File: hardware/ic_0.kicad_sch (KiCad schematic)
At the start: 24 parts, among them IC1 BTS722204ESAXUMA1

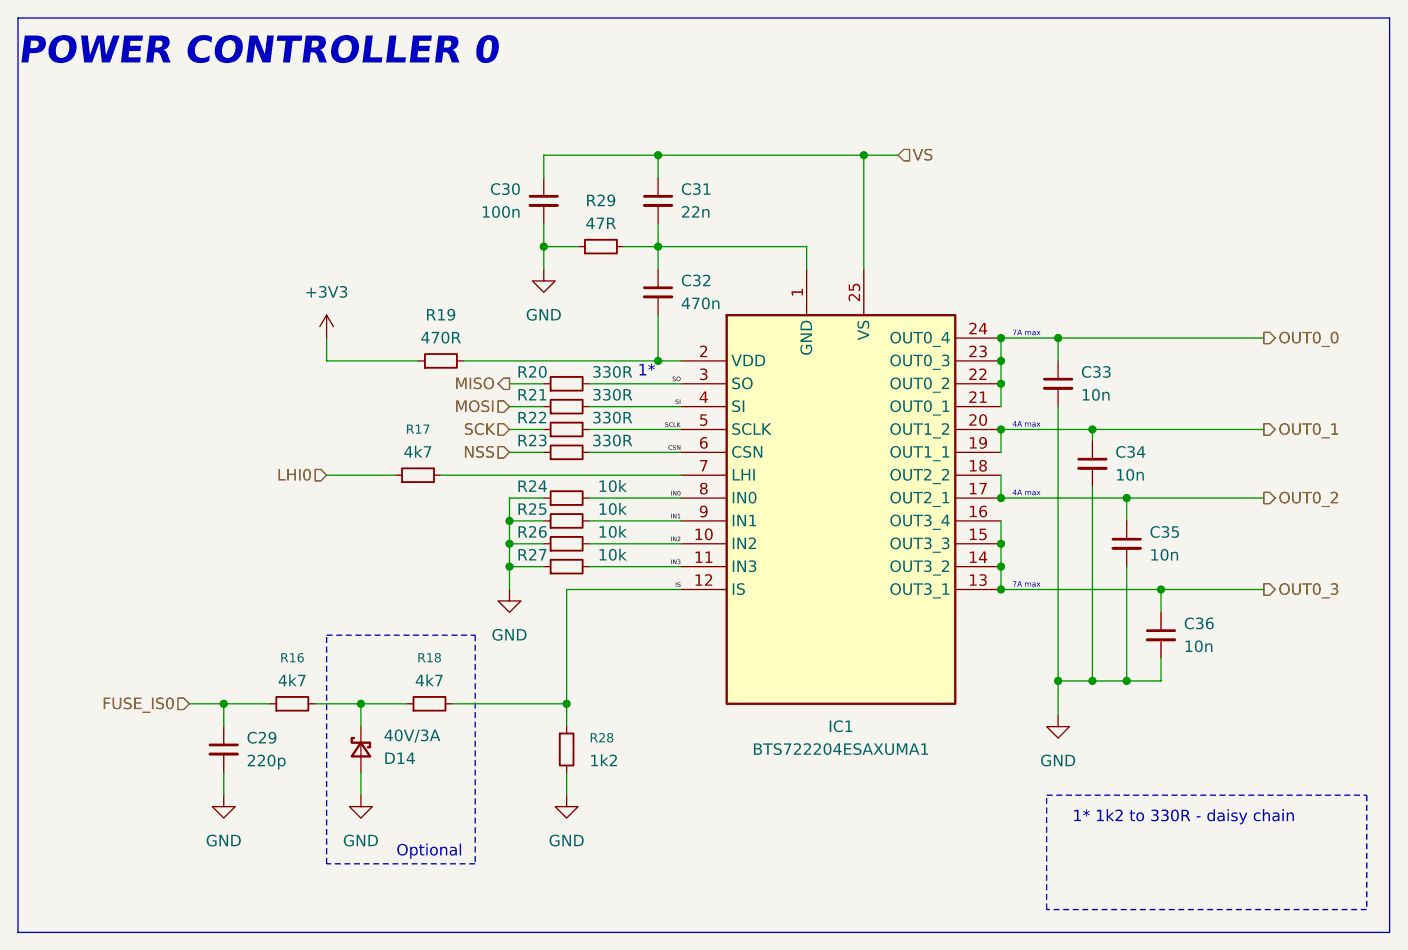
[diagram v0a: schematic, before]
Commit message: new pcb layout & can coppied from steeringwheel
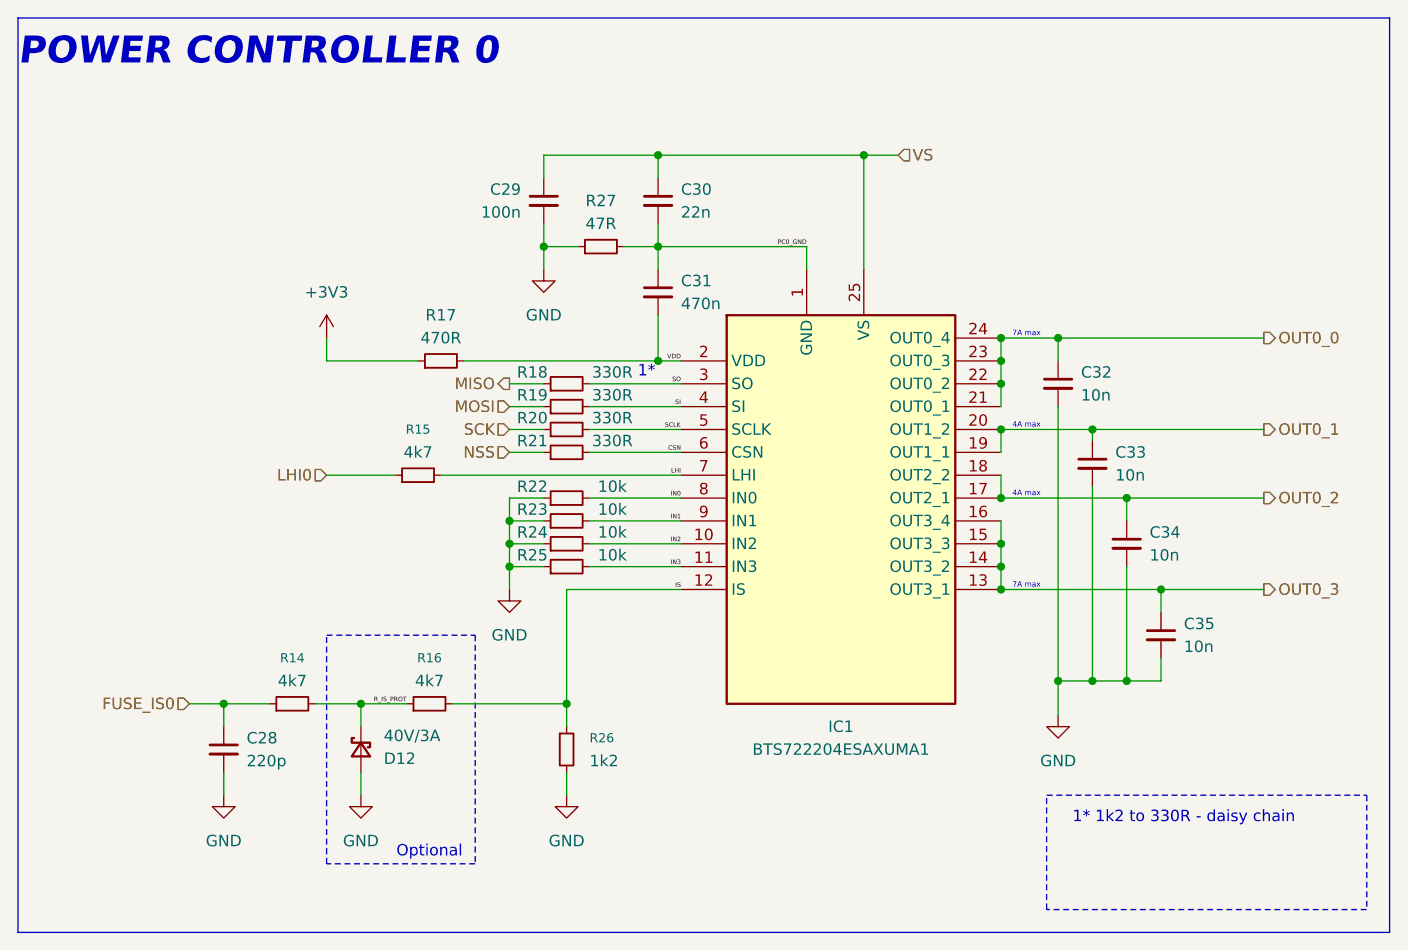
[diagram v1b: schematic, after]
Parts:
- renumbered C29 to C28, C30 to C29, C31 to C30, C32 to C31, C33 to C32, C34 to C33, C35 to C34, C36 to C35, D14 to D12, R16 to R14, R17 to R15, R18 to R16, R19 to R17, R20 to R18, R21 to R19, R22 to R20, R23 to R21, R24 to R22, R25 to R23, R26 to R24, R27 to R25, R28 to R26, R29 to R27
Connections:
- net R_IS_PROT: now reaches D12.1 (K), R14.2, R16.1
- net LHI: now reaches IC1.7 (LHI), R15.2
- net PC0_GND: now reaches C30.2, C31.1, IC1.1 (GND), R27.2
- net VDD: now reaches C31.2, IC1.2 (VDD), R17.2
